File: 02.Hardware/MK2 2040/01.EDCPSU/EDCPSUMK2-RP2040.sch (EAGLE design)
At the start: 208 parts, among them J1 DX07S016JA1R1500, J6 Display, K1 FLEX CONNECTORES, Q2 2N7002PW, Q4 2N7002PW, Q5 2N7002PW, Q9 2N7002PW, U1 RP2040TR7, U10 IP2721, U11 AP63203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

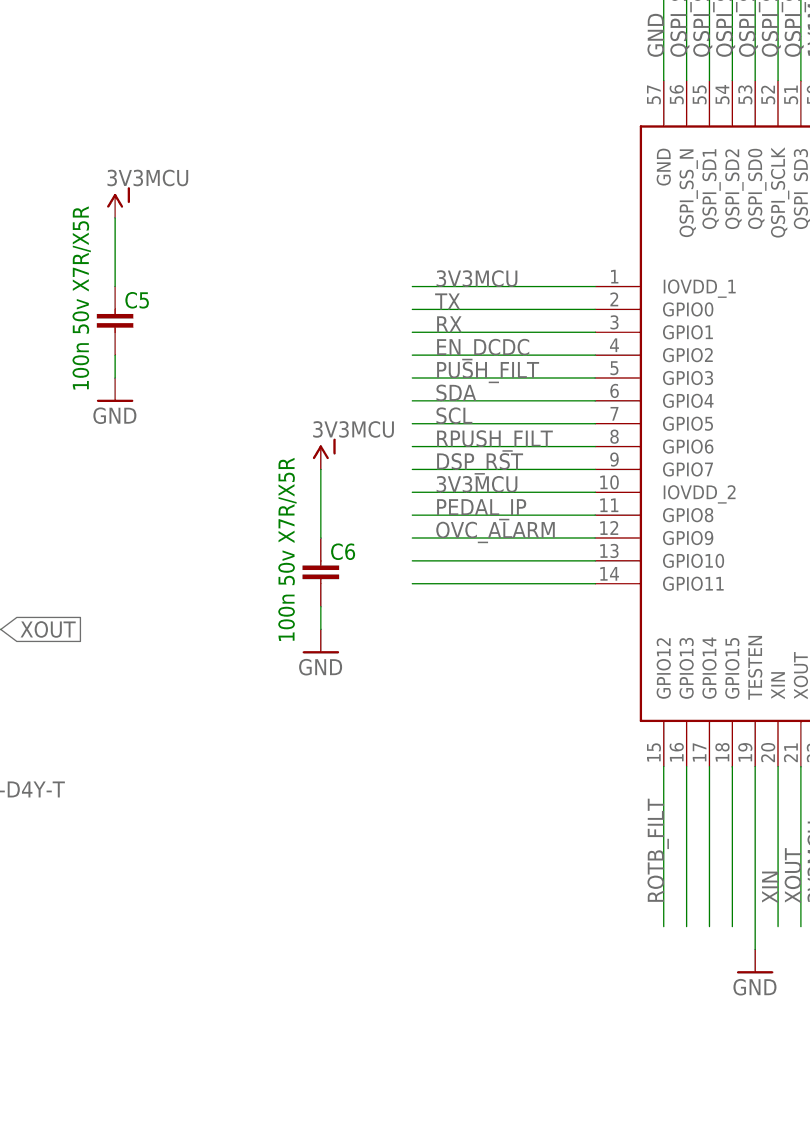
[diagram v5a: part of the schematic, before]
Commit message: Fallo en el I2C. #Issue 15
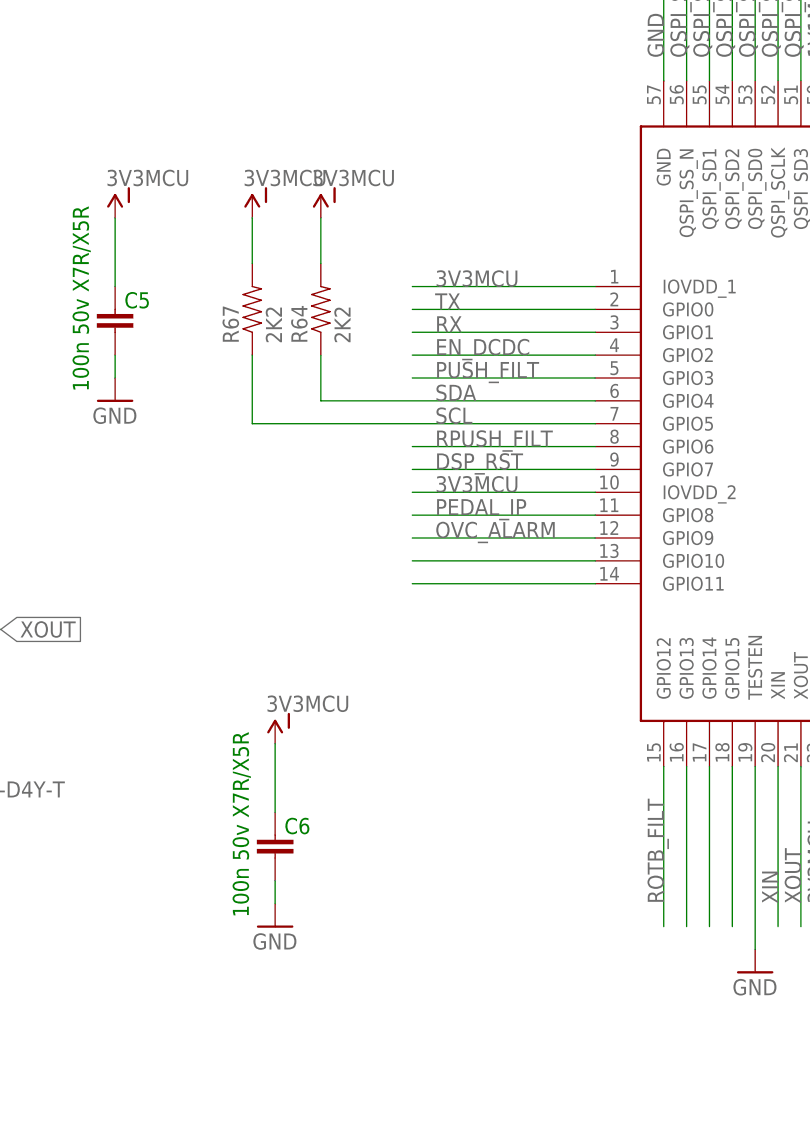
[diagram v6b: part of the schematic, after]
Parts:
- added R64, R67: 2K2, SparkFun-Resistors:RESISTOR0805
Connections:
- net 3V3MCU: now also R64.2, R67.2
- net SCL: now also R67.1
- net SDA: now also R64.1
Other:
- moved on the sheet: C6
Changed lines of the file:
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@@
 <part name="SEL" library="BeagleBone_Blue_R3" deviceset="TESTPAD_TPSQ" device="B1,27"/>
 <part name="D1" library="3SMAJ5934B" deviceset="3SMAJ5934B" device="" value="SMAJ24A"/>
+<part name="R64" library="SparkFun-Resistors" library_urn="urn:adsk.eagle:library:532" deviceset="RESISTOR" device="0805" package3d_urn="urn:adsk.eagle:package:39651/1" value="2K2"/>
+<part name="R67" library="SparkFun-Resistors" library_urn="urn:adsk.eagle:library:532" deviceset="RESISTOR" device="0805" package3d_urn="urn:adsk.eagle:package:39651/1" value="2K2"/>
+<part name="U$42" library="SparkFun-Aesthetics" deviceset="VCC-ISO" device="" value="3V3MCU"/>
+<part name="U$43" library="SparkFun-Aesthetics" deviceset="VCC-ISO" device="" value="3V3MCU"/>
 </parts>
 <sheets>
@@
 <attribute name="VALUE" x="-267.081" y="216.916" size="1.778" layer="91" rot="R90"/>
 </instance>
-<instance part="C6" gate="G$1" x="-241.3" y="198.12" smashed="yes" rot="R180">
-<attribute name="NAME" x="-240.284" y="198.247" size="1.778" layer="91"/>
-<attribute name="VALUE" x="-244.221" y="188.976" size="1.778" layer="91" rot="R90"/>
+<instance part="C6" gate="G$1" x="-246.38" y="167.64" smashed="yes" rot="R180">
+<attribute name="NAME" x="-245.364" y="167.767" size="1.778" layer="91"/>
+<attribute name="VALUE" x="-249.301" y="158.496" size="1.778" layer="91" rot="R90"/>
 </instance>
 <instance part="C7" gate="G$1" x="-114.3" y="200.66" smashed="yes" rot="R180">
@@
 <attribute name="VALUE" x="-266.7" y="213.36" size="1.778" layer="96"/>
 </instance>
-<instance part="GND63" gate="1" x="-241.3" y="187.96" smashed="yes">
-<attribute name="VALUE" x="-243.84" y="185.42" size="1.778" layer="96"/>
+<instance part="GND63" gate="1" x="-246.38" y="157.48" smashed="yes">
+<attribute name="VALUE" x="-248.92" y="154.94" size="1.778" layer="96"/>
 </instance>
 <instance part="GND68" gate="1" x="-193.04" y="152.4" smashed="yes">
@@
 <attribute name="VALUE" x="-111.76" y="238.76" size="1.778" layer="96"/>
 </instance>
-<instance part="U$15" gate="G$1" x="-241.3" y="208.28" smashed="yes">
-<attribute name="VALUE" x="-242.316" y="211.836" size="1.778" layer="96"/>
+<instance part="U$15" gate="G$1" x="-246.38" y="177.8" smashed="yes">
+<attribute name="VALUE" x="-247.396" y="181.356" size="1.778" layer="96"/>
 </instance>
 <instance part="U$41" gate="G$1" x="-96.52" y="208.28" smashed="yes">
@@
 <attribute name="NAME" x="-177.8" y="-25.4" size="1.778" layer="95" rot="R180"/>
 <attribute name="VALUE" x="-177.8" y="-29.21" size="1.778" layer="96" rot="R180"/>
+</instance>
+<instance part="R64" gate="G$1" x="-241.3" y="226.06" smashed="yes" rot="R90">
+<attribute name="NAME" x="-242.7986" y="222.25" size="1.778" layer="95" rot="R90"/>
+<attribute name="VALUE" x="-237.998" y="222.25" size="1.778" layer="96" rot="R90"/>
+</instance>
+<instance part="R67" gate="G$1" x="-248.92" y="226.06" smashed="yes" rot="R90">
+<attribute name="NAME" x="-250.4186" y="222.25" size="1.778" layer="95" rot="R90"/>
+<attribute name="VALUE" x="-245.618" y="222.25" size="1.778" layer="96" rot="R90"/>
+</instance>
+<instance part="U$42" gate="G$1" x="-248.92" y="236.22" smashed="yes">
+<attribute name="VALUE" x="-249.936" y="239.776" size="1.778" layer="96"/>
+</instance>
+<instance part="U$43" gate="G$1" x="-241.3" y="236.22" smashed="yes">
+<attribute name="VALUE" x="-242.316" y="239.776" size="1.778" layer="96"/>
 </instance>
 </instances>
@@
 <pinref part="GND63" gate="1" pin="GND"/>
 <pinref part="C6" gate="G$1" pin="1"/>
-<wire x1="-241.3" y1="190.5" x2="-241.3" y2="193.04" width="0.1524" layer="91"/>
+<wire x1="-246.38" y1="160.02" x2="-246.38" y2="162.56" width="0.1524" layer="91"/>
 </segment>
 <segment>
@@
 <segment>
 <pinref part="U1" gate="G$1" pin="GPIO5"/>
-<wire x1="-210.82" y1="213.36" x2="-231.14" y2="213.36" width="0.1524" layer="91"/>
+<wire x1="-210.82" y1="213.36" x2="-248.92" y2="213.36" width="0.1524" layer="91"/>
 <label x="-228.6" y="213.36" size="1.778" layer="95"/>
+<pinref part="R67" gate="G$1" pin="1"/>
+<wire x1="-248.92" y1="213.36" x2="-248.92" y2="220.98" width="0.1524" layer="91"/>
 </segment>
 <segment>
@@
 <segment>
 <pinref part="U1" gate="G$1" pin="GPIO4"/>
-<wire x1="-210.82" y1="215.9" x2="-231.14" y2="215.9" width="0.1524" layer="91"/>
+<wire x1="-210.82" y1="215.9" x2="-241.3" y2="215.9" width="0.1524" layer="91"/>
 <label x="-228.6" y="215.9" size="1.778" layer="95"/>
+<pinref part="R64" gate="G$1" pin="1"/>
+<wire x1="-241.3" y1="215.9" x2="-241.3" y2="220.98" width="0.1524" layer="91"/>
 </segment>
 <segment>
@@
 <segment>
 <pinref part="C6" gate="G$1" pin="2"/>
-<wire x1="-241.3" y1="200.66" x2="-241.3" y2="208.28" width="0.1524" layer="91"/>
+<wire x1="-246.38" y1="170.18" x2="-246.38" y2="177.8" width="0.1524" layer="91"/>
 <pinref part="U$15" gate="G$1" pin="VCC-ISO"/>
 </segment>
@@
 <junction x="-106.68" y="106.68"/>
 </segment>
-</net>
+<segment>
+<pinref part="U$42" gate="G$1" pin="VCC-ISO"/>
+<pinref part="R67" gate="G$1" pin="2"/>
+<wire x1="-248.92" y1="236.22" x2="-248.92" y2="231.14" width="0.1524" layer="91"/>
+</segment>
+<segment>
+<pinref part="U$43" gate="G$1" pin="VCC-ISO"/>
+<pinref part="R64" gate="G$1" pin="2"/>
+<wire x1="-241.3" y1="236.22" x2="-241.3" y2="231.14" width="0.1524" layer="91"/>
+</segment>
+</net>

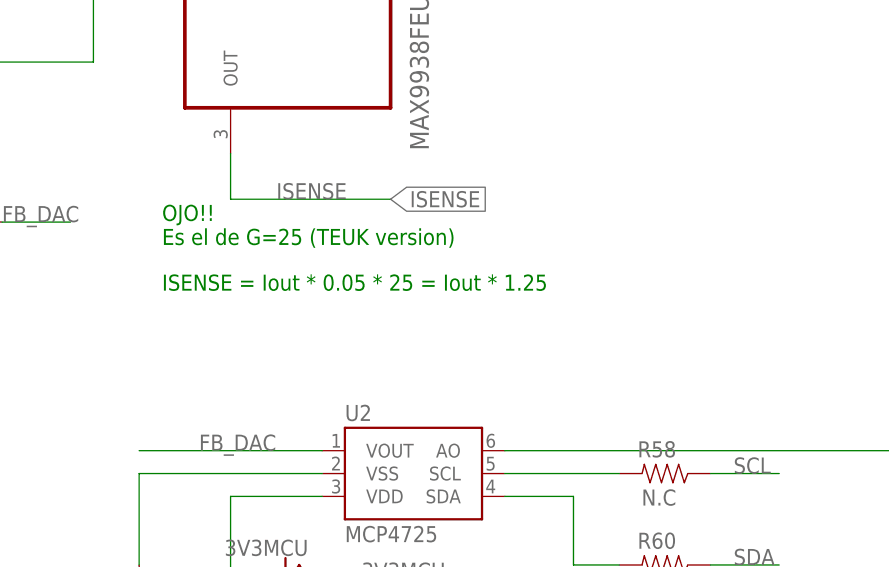
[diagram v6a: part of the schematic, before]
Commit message: Issue #18
Version 1 de la propuesta de cambio
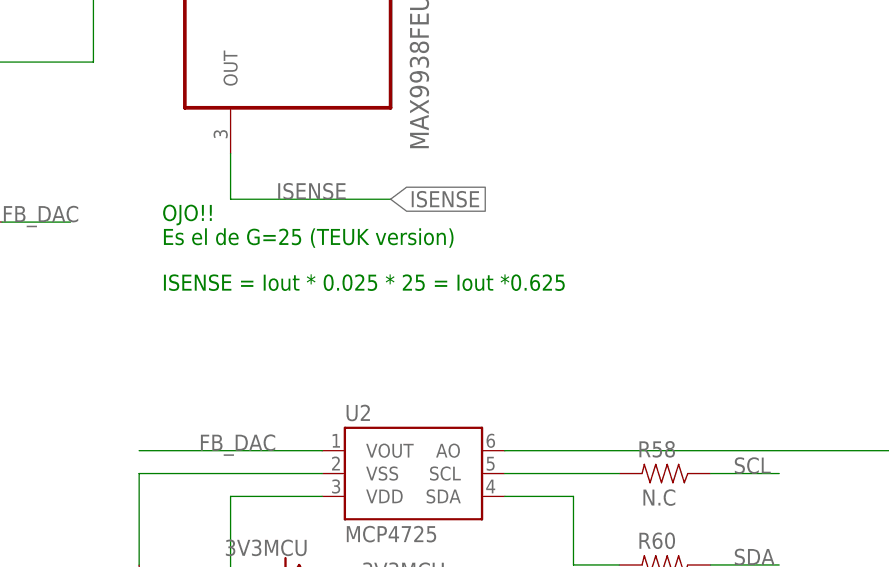
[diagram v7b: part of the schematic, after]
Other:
- note added: "ISENSE = Iout * 0.025 * 25 = Iout *0.625"
- note removed: "ISENSE = Iout * 0.05 * 25 = Iout * 1.25"
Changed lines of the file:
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@@
 <text x="469.9" y="177.8" size="1.778" layer="91">OJO!!
 Es el de G=25 (TEUK version)</text>
-<text x="469.9" y="172.72" size="1.778" layer="91">ISENSE = Iout * 0.05 * 25 = Iout * 1.25</text>
+<text x="469.9" y="172.72" size="1.778" layer="91">ISENSE = Iout * 0.025 * 25 = Iout *0.625</text>
 <text x="-447.04" y="284.48" size="6.4516" layer="94">FLEX Connectors</text>
 <text x="-431.8" y="-60.96" size="1.778" layer="91">3V @ Vi=25V</text>
